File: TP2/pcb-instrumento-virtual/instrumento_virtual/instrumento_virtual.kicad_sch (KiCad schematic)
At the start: 70 parts, among them J1 Conn_01x09_Pin, J2 Conector_salidas_analógicas, J3 Conn_01x20_Socket, J4 Conn_01x09_Pin, J5 Conn_01x20_Socket, J7 RS232, Q3 BC547, U1 CD4051B, U2 MCP6002-xMC, U3 ULN2003, U4 AMS1117-3.3, U5 AMS1117-5.0, U6 MCP6002-xMC

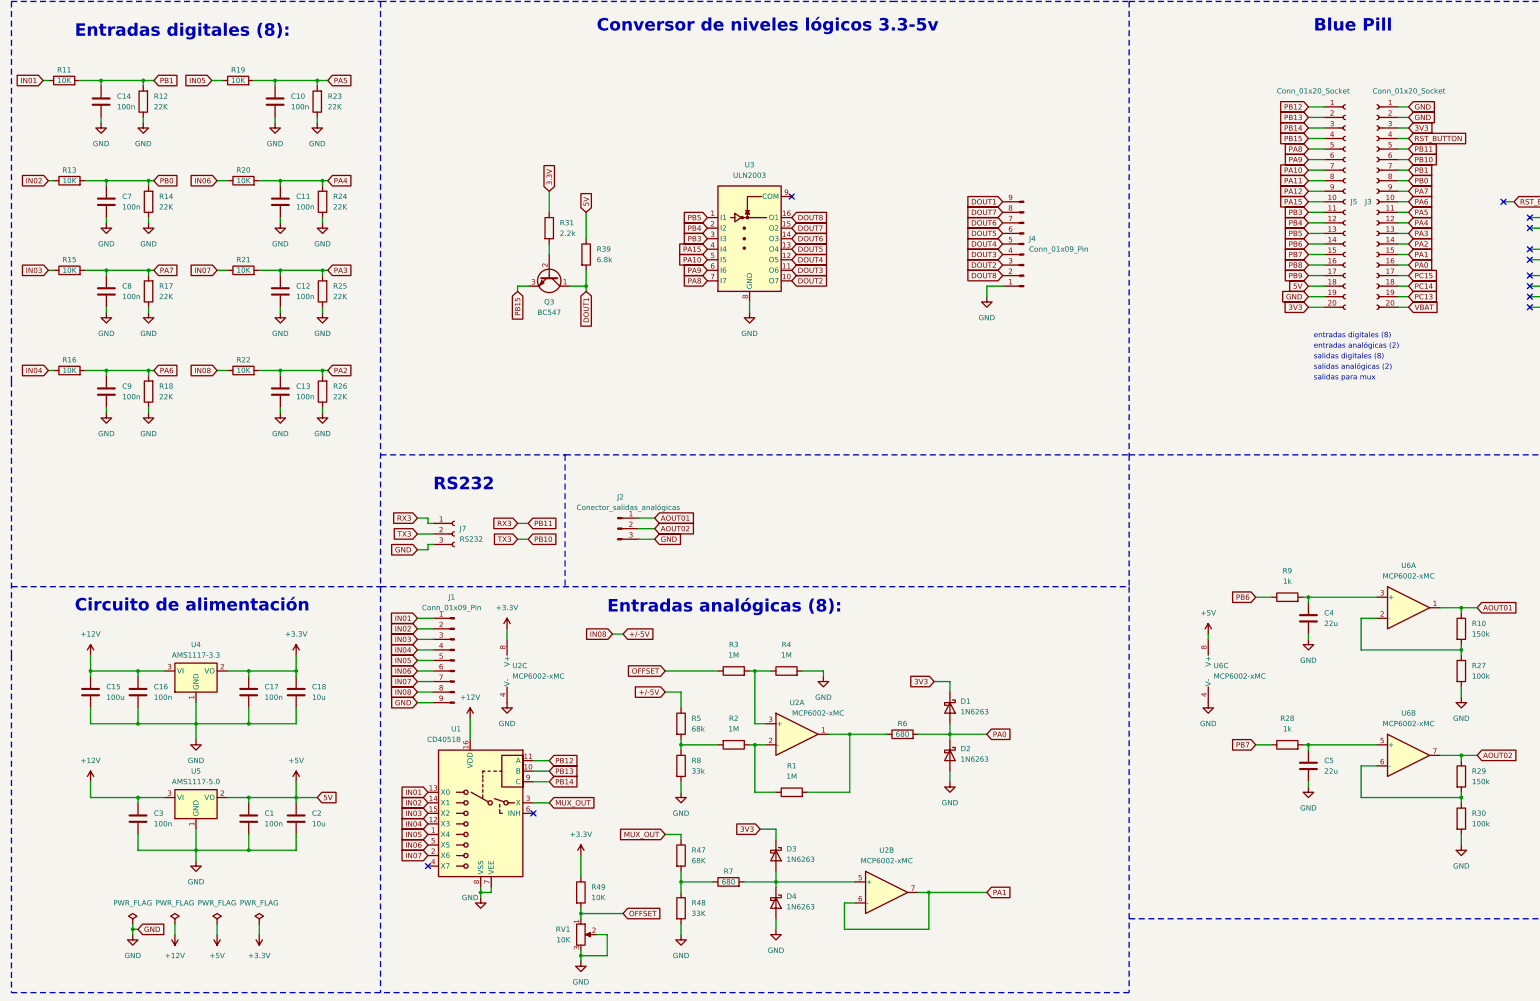
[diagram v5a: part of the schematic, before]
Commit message: pcb actualizada
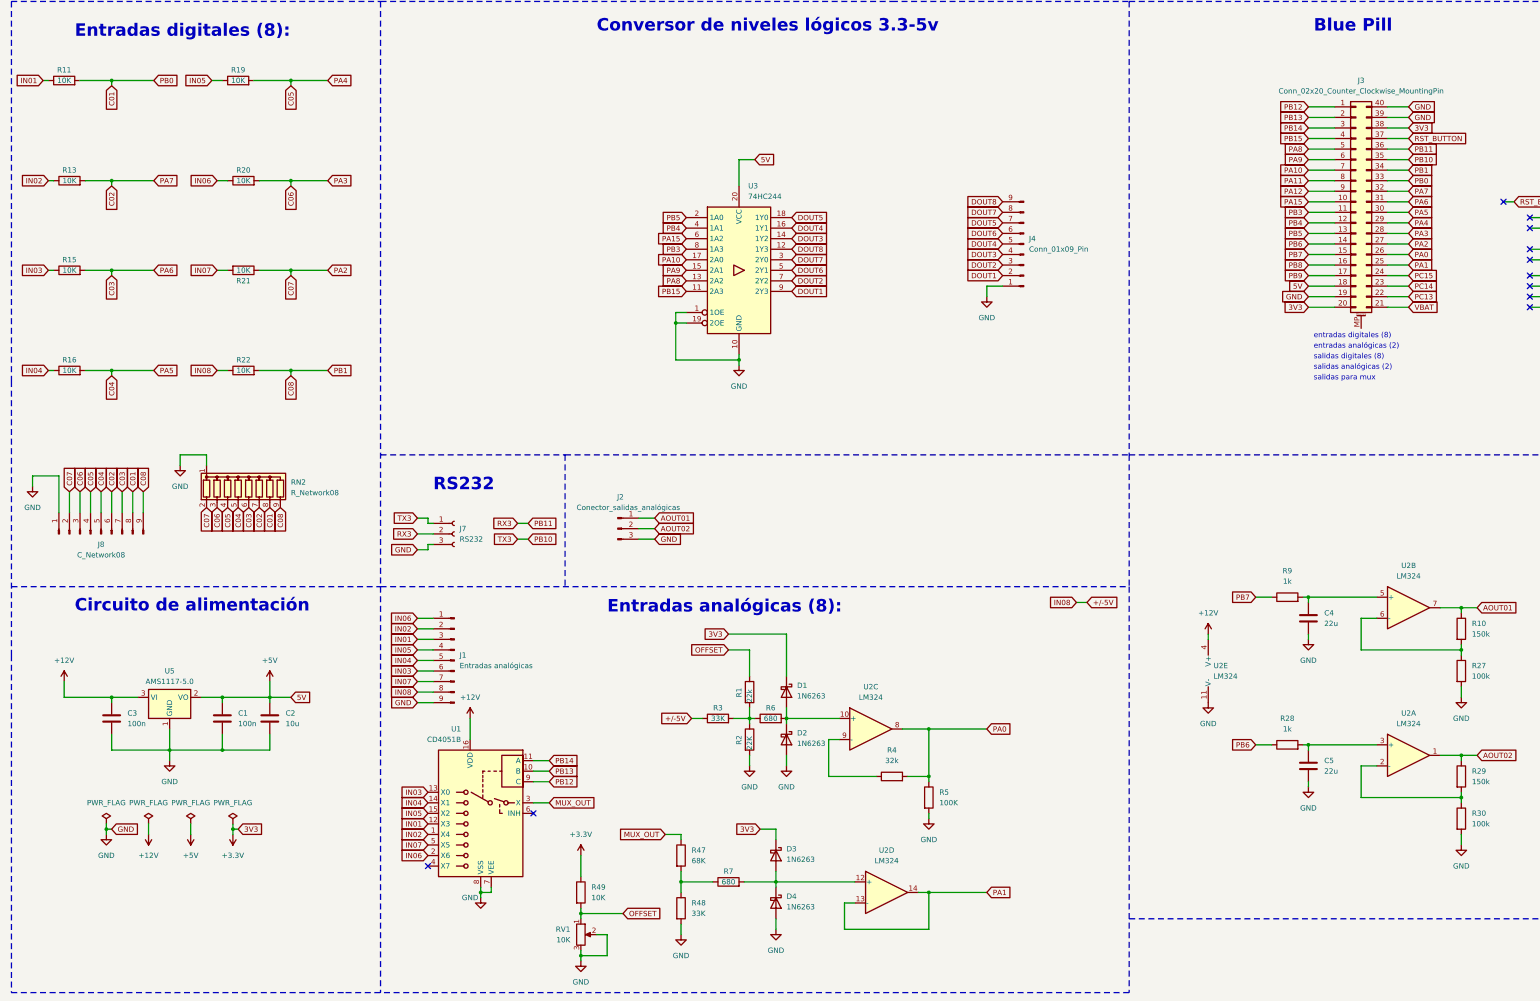
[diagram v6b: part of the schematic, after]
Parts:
- removed C10, C11, C12, C13, C14, C16, C17, C7, C8, C9: 100n, Capacitor_THT:C_Disc_D6.0mm_W2.5mm_P5.00mm, symbol Device:C
- removed C15: 100u, Capacitor_THT:CP_Radial_D6.3mm_P2.50mm, symbol Device:C
- removed C18: 10u, Capacitor_THT:CP_Radial_D5.0mm_P2.50mm, symbol Device:C
- removed J3, J5: Conn_01x20_Socket, Connector_PinHeader_2.54mm:PinHeader_1x20_P2.54mm_Vertical, symbol Connector:Conn_01x20_Socket
- removed Q3: BC547, Package_TO_SOT_THT:TO-92_Inline, symbol Transistor_BJT:BC547
- removed R12, R14, R17, R18, R23, R24, R25, R26: 22K, Resistor_THT:R_Box_L8.4mm_W2.5mm_P5.08mm, symbol Device:R
- removed R31: 2.2k, Resistor_THT:R_Box_L8.4mm_W2.5mm_P5.08mm, symbol Device:R
- removed R39: 6.8k, Resistor_THT:R_Box_L8.4mm_W2.5mm_P5.08mm, symbol Device:R
- removed R8: 33k, Resistor_THT:R_Box_L8.4mm_W2.5mm_P5.08mm, symbol Device:R
- removed U2, U6: MCP6002-xMC, Package_DIP:DIP-8_W7.62mm, symbol Amplifier_Operational:MCP6002-xMC
- removed U3: ULN2003, Package_DIP:DIP-16_W7.62mm_LongPads, symbol Transistor_Array:ULN2003
- removed U4: AMS1117-3.3, Package_TO_SOT_SMD:SOT-223-3_TabPin2, symbol Regulator_Linear:AMS1117-3.3
- added J3: Conn_02x20_Counter_Clockwise_MountingPin, Package_DIP:DIP-40_W15.24mm_LongPads, symbol Connector_Generic_MountingPin:Conn_02x20_Counter_Clockwise_MountingPin
- added J8: C_Network08, Connector_PinHeader_2.54mm:PinHeader_1x09_P2.54mm_Vertical, symbol Connector:Conn_01x09_Pin
- added RN2: R_Network08, Resistor_THT:R_Array_SIP9, symbol Device:R_Network08
- added U2: LM324, Package_DIP:DIP-14_W7.62mm, symbol Amplifier_Operational:LM324
- added U3: 74HC244, Package_DIP:DIP-20_W7.62mm, symbol 74xx:74HC244
- J1: value Conn_01x09_Pin -> Entradas analógicas
- R1: value 1M -> 22k; footprint Resistor_THT:R_Box_L8.4mm_W2.5mm_P5.08mm -> Resistor_THT:R_Axial_DIN0309_L9.0mm_D3.2mm_P12.70mm_Horizontal
- R10, R11, R13, R15, R16, R19, R20, R21, R22, R27, R28, R29, R30, R47, R48, R49, R6, R7, R9: footprint Resistor_THT:R_Box_L8.4mm_W2.5mm_P5.08mm -> Resistor_THT:R_Axial_DIN0309_L9.0mm_D3.2mm_P12.70mm_Horizontal
- R2: value 1M -> 22K; footprint Resistor_THT:R_Box_L8.4mm_W2.5mm_P5.08mm -> Resistor_THT:R_Axial_DIN0309_L9.0mm_D3.2mm_P12.70mm_Horizontal
- R3: value 1M -> 33K; footprint Resistor_THT:R_Box_L8.4mm_W2.5mm_P5.08mm -> Resistor_THT:R_Axial_DIN0309_L9.0mm_D3.2mm_P12.70mm_Horizontal
- R4: value 1M -> 32k; footprint Resistor_THT:R_Box_L8.4mm_W2.5mm_P5.08mm -> Resistor_THT:R_Axial_DIN0309_L9.0mm_D3.2mm_P12.70mm_Horizontal
- R5: value 68k -> 100K; footprint Resistor_THT:R_Box_L8.4mm_W2.5mm_P5.08mm -> Resistor_THT:R_Axial_DIN0309_L9.0mm_D3.2mm_P12.70mm_Horizontal
- RV1: footprint Resistor_THT:R_Box_L8.4mm_W2.5mm_P5.08mm -> Potentiometer_THT:Potentiometer_Bourns_3266Y_Vertical
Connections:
- net 3V3 is gone; now on net +3.3V: D1.1 (K), D3.1 (K)
- net PA3 is gone; now on net IN07: R21.2
- net +12V: now also U2.4 (V+)
- net +3.3V: now also J3.20 (Pin_20), J3.38 (Pin_38)
- net +5V: now also J3.18 (Pin_18), U3.20 (VCC)
- net +/-5V: now also R3.1; no longer R5.1
- net AOUT01: now also U2.7
- net AOUT02: now also U2.1
- net DOUT1: now also J4.2 (Pin_2), U3.9 (2Y3); no longer J4.9 (Pin_9)
- net DOUT2: now also U3.7 (2Y2)
- net DOUT3: now also U3.14 (1Y2)
- net DOUT4: now also U3.16 (1Y1)
- net DOUT5: now also J4.7 (Pin_7), U3.18 (1Y0); no longer J4.6 (Pin_6)
- net DOUT6: now also J4.6 (Pin_6), U3.5 (2Y1); no longer J4.7 (Pin_7)
- net DOUT7: now also U3.3 (2Y0)
- net DOUT8: now also J4.9 (Pin_9), U3.12 (1Y3); no longer J4.2 (Pin_2)
- net GND: now also R2.2, R5.2, J3.19 (Pin_19), J3.39 (Pin_39), J3.40 (Pin_40), J8.1 (Pin_1), RN2.1 (common), U2.11 (V-), U3.1 (1OE), U3.10 (GND), U3.19 (2OE); no longer R4.2
- net IN01: now also J1.3 (Pin_3), U1.12 (X3); no longer J1.1 (Pin_1), U1.13 (X0)
- net IN02: now also U1.1 (X4); no longer U1.14 (X1)
- net IN03: now also J1.6 (Pin_6), U1.13 (X0); no longer J1.3 (Pin_3), U1.15 (X2)
- net IN04: now also J1.5 (Pin_5), U1.14 (X1); no longer J1.4 (Pin_4), U1.12 (X3)
- net IN05: now also J1.4 (Pin_4), U1.15 (X2); no longer J1.5 (Pin_5), U1.1 (X4)
- net IN06: now also J1.1 (Pin_1), U1.2 (X6); no longer J1.6 (Pin_6), U1.5 (X5)
- net IN07: now also U1.5 (X5); no longer R21.1, U1.2 (X6)
- net OFFSET: now also R1.1; no longer R3.1
- net PA0: now also R4.2, R5.1, J3.26 (Pin_26), U2.8; no longer D1.2 (A), D2.1 (K), R6.2
- net PA1: now also J3.25 (Pin_25), U2.13 (-), U2.14
- net PA10: now also J3.7 (Pin_7), U3.17 (2A0)
- net PA11: now also J3.8 (Pin_8)
- net PA12: now also J3.9 (Pin_9)
- net PA15: now also J3.10 (Pin_10), U3.6 (1A2)
- net PA8: now also J3.5 (Pin_5), U3.13 (2A2)
- net PA9: now also J3.6 (Pin_6), U3.15 (2A1)
- net PB10: now also J7.1 (Pin_1), J3.35 (Pin_35); no longer J7.2 (Pin_2)
- net PB11: now also J7.2 (Pin_2), J3.36 (Pin_36); no longer J7.1 (Pin_1)
- net PB12: now also U1.9 (C), J3.1 (Pin_1); no longer U1.11 (A)
- net PB13: now also J3.2 (Pin_2)
- net PB14: now also U1.11 (A), J3.3 (Pin_3); no longer U1.9 (C)
- net PB15: now also J3.4 (Pin_4), U3.11 (2A3)
- net PB3: now also J3.11 (Pin_11), U3.8 (1A3)
- net PB4: now also J3.12 (Pin_12), U3.4 (1A1)
- net PB5: now also J3.13 (Pin_13), U3.2 (1A0)
- net PB6: now also R28.1, J3.14 (Pin_14); no longer R9.1
- net PB7: now also R9.1, J3.15 (Pin_15); no longer R28.1
- net PB8: now also J3.16 (Pin_16)
- net PB9: now also J3.17 (Pin_17)
- net PC13: now also J3.22 (Pin_22)
- net PC14: now also J3.23 (Pin_23)
- net PC15: now also J3.24 (Pin_24)
- net RST_BUTTON: now also J3.37 (Pin_37)
- net VBAT: now also J3.21 (Pin_21)
- net at C4.1, R9.2: now also U2.5 (+)
- net at R2.1: now also R1.2, R3.2, R6.1; no longer R1.1
- net at R4.1: now also U2.9 (-); no longer R3.2
- net at R29.2, R30.1: now also U2.2 (-)
- net at D3.2 (A), D4.1 (K), R7.2: now also U2.12 (+)
- net at C5.1, R28.2: now also U2.3 (+)
- net at R10.2, R27.1: now also U2.6 (-)
- net PA2 renamed C08
- net C08: now also J3.34 (Pin_34), J8.9 (Pin_9), RN2.9 (R8)
- net PA4 renamed C06
- net C06: now also J3.28 (Pin_28), J8.3 (Pin_3), RN2.3 (R2)
- net PA5 renamed C05
- net C05: now also J3.29 (Pin_29), J8.4 (Pin_4), RN2.4 (R3)
- net PA6 renamed C04
- net C04: now also J3.30 (Pin_30), J8.5 (Pin_5), RN2.5 (R4)
- net PA7 renamed C03
- net C03: now also J3.31 (Pin_31), J8.7 (Pin_7), RN2.6 (R5)
- net PB0 renamed C02
- net C02: now also J3.32 (Pin_32), J8.6 (Pin_6), RN2.7 (R6)
- net PB1 renamed C01
- net C01: now also J3.33 (Pin_33), J8.8 (Pin_8), RN2.8 (R7)
- new net: D1.2 (A), D2.1 (K), R6.2, U2.10 (+)
- new net C07: J3.27 (Pin_27), J8.2 (Pin_2), R21.1, RN2.2 (R1)
- no-connect marks 12 -> 11
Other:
- moved on the sheet: C1, C2, C3, D1, D2, R21, U5

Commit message: version final pcb
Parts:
- removed R49: 10K, Resistor_THT:R_Axial_DIN0309_L9.0mm_D3.2mm_P12.70mm_Horizontal, symbol Device:R
- added J6: Conn_01x02, Connector_PinSocket_2.54mm:PinSocket_2x01_P2.54mm_Vertical, symbol Connector_Generic:Conn_01x02
- added R8: 15K, Resistor_THT:R_Axial_DIN0309_L9.0mm_D3.2mm_P12.70mm_Horizontal, symbol Device:R
- added RN1: R_Network08, Resistor_THT:R_Array_SIP9, symbol Device:R_Network08
- added U4: TL082, Package_DIP:DIP-8_W7.62mm, symbol Amplifier_Operational:TL082
- C1: footprint Capacitor_THT:C_Disc_D6.0mm_W2.5mm_P5.00mm -> Capacitor_THT:C_Disc_D9.0mm_W2.5mm_P5.00mm
- C2, C4, C5: footprint Capacitor_THT:CP_Radial_D5.0mm_P2.50mm -> Capacitor_THT:CP_Radial_D8.0mm_P5.00mm
- C3: footprint Capacitor_THT:CP_Radial_D5.0mm_P2.50mm -> Capacitor_THT:C_Disc_D9.0mm_W2.5mm_P5.00mm
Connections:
- net +12V: now also J6.2 (Pin_2), U4.8 (V+)
- net +3.3V: now also R8.1, RN1.1 (common)
- net C02: now also J8.7 (Pin_7); no longer J8.6 (Pin_6)
- net C03: now also J8.6 (Pin_6); no longer J8.7 (Pin_7)
- net GND: now also U1.6 (INH), J6.1 (Pin_1), U4.4 (V-), U4.5 (+), U4.6 (-), U4.7
- net OFFSET: now also U4.1, U4.2 (-); no longer RV1.1
- net PA10: now also U3.6 (1A2), RN1.6 (R5); no longer U3.17 (2A0)
- net PA15: now also U3.17 (2A0), RN1.4 (R3); no longer U3.6 (1A2)
- net PA8: now also RN1.8 (R7)
- net PA9: now also RN1.7 (R6)
- net PB15: now also RN1.9 (R8)
- net PB3: now also RN1.5 (R4)
- net PB4: now also RN1.3 (R2)
- net PB5: now also RN1.2 (R1)
- new net: R8.2, RV1.1, U4.3 (+)
- no-connect marks 11 -> 10
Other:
- note added: "Salidas analógicas (2):"
- moved on the sheet: J2
